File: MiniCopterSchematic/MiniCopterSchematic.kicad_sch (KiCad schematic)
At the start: 19 parts, among them J1 MPU6050_IMU, M1 MOTOR_DC_1, M2 MOTOR_DC_2, M3 MOTOR_DC_3, M4 MOTOR_DC_4, Q1 FQP20NO6L, Q2 FQP20NO6L, Q3 FQP20NO6L, Q4 FQP20NO6L

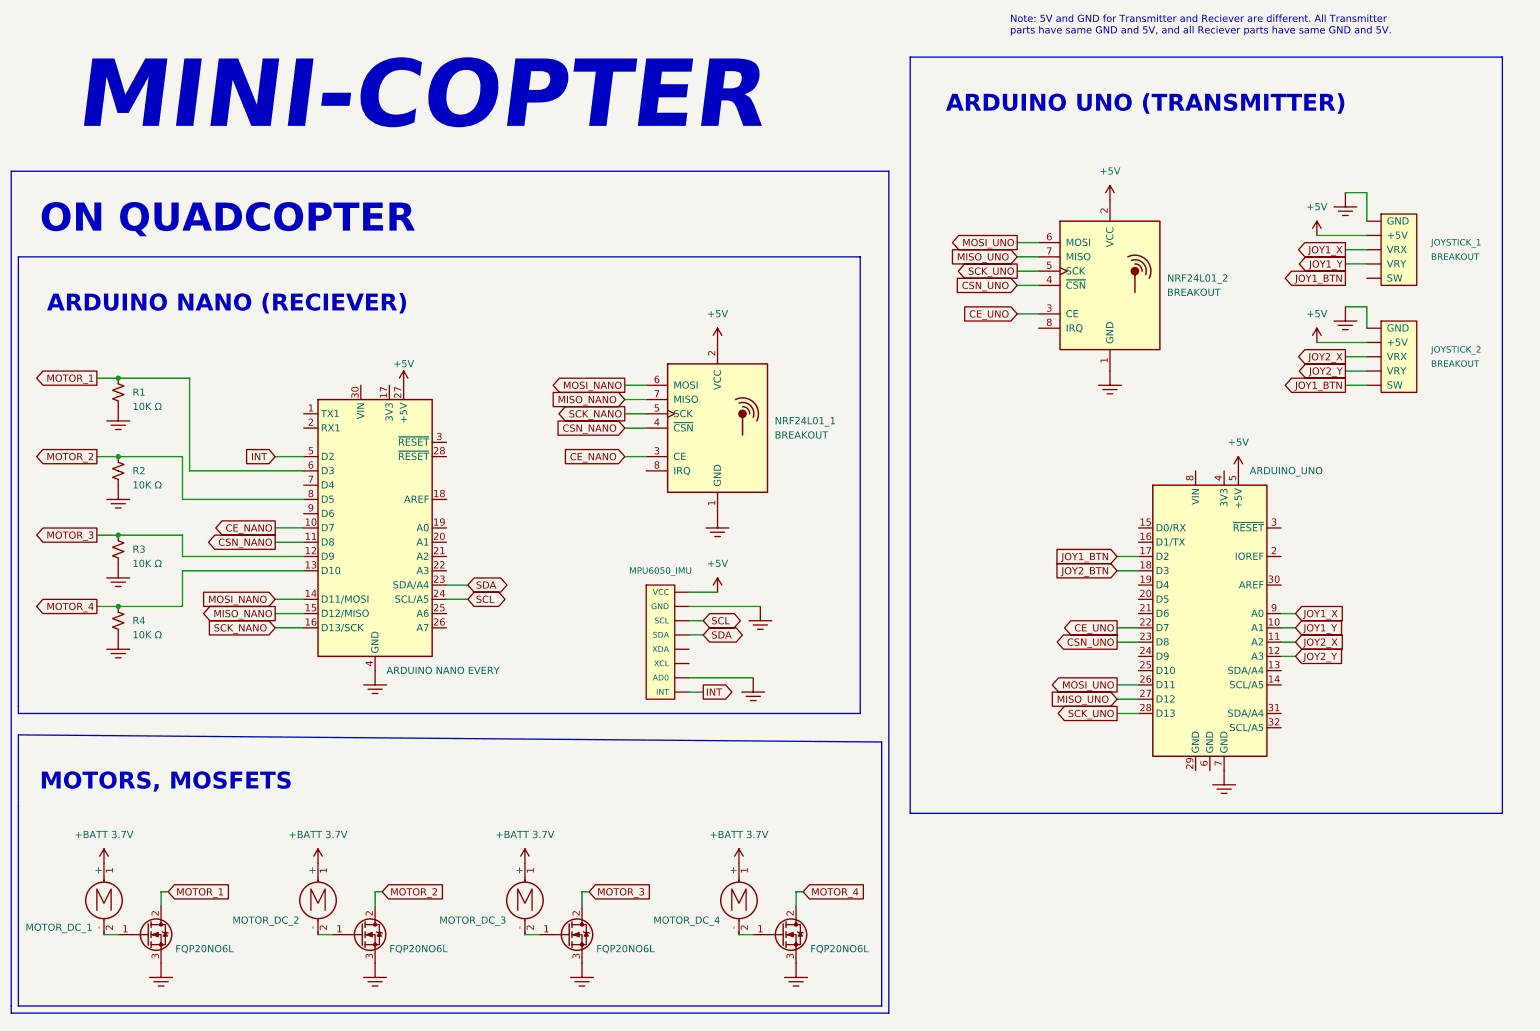
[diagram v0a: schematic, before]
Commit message: Updated schematic, added pictures, updated readme
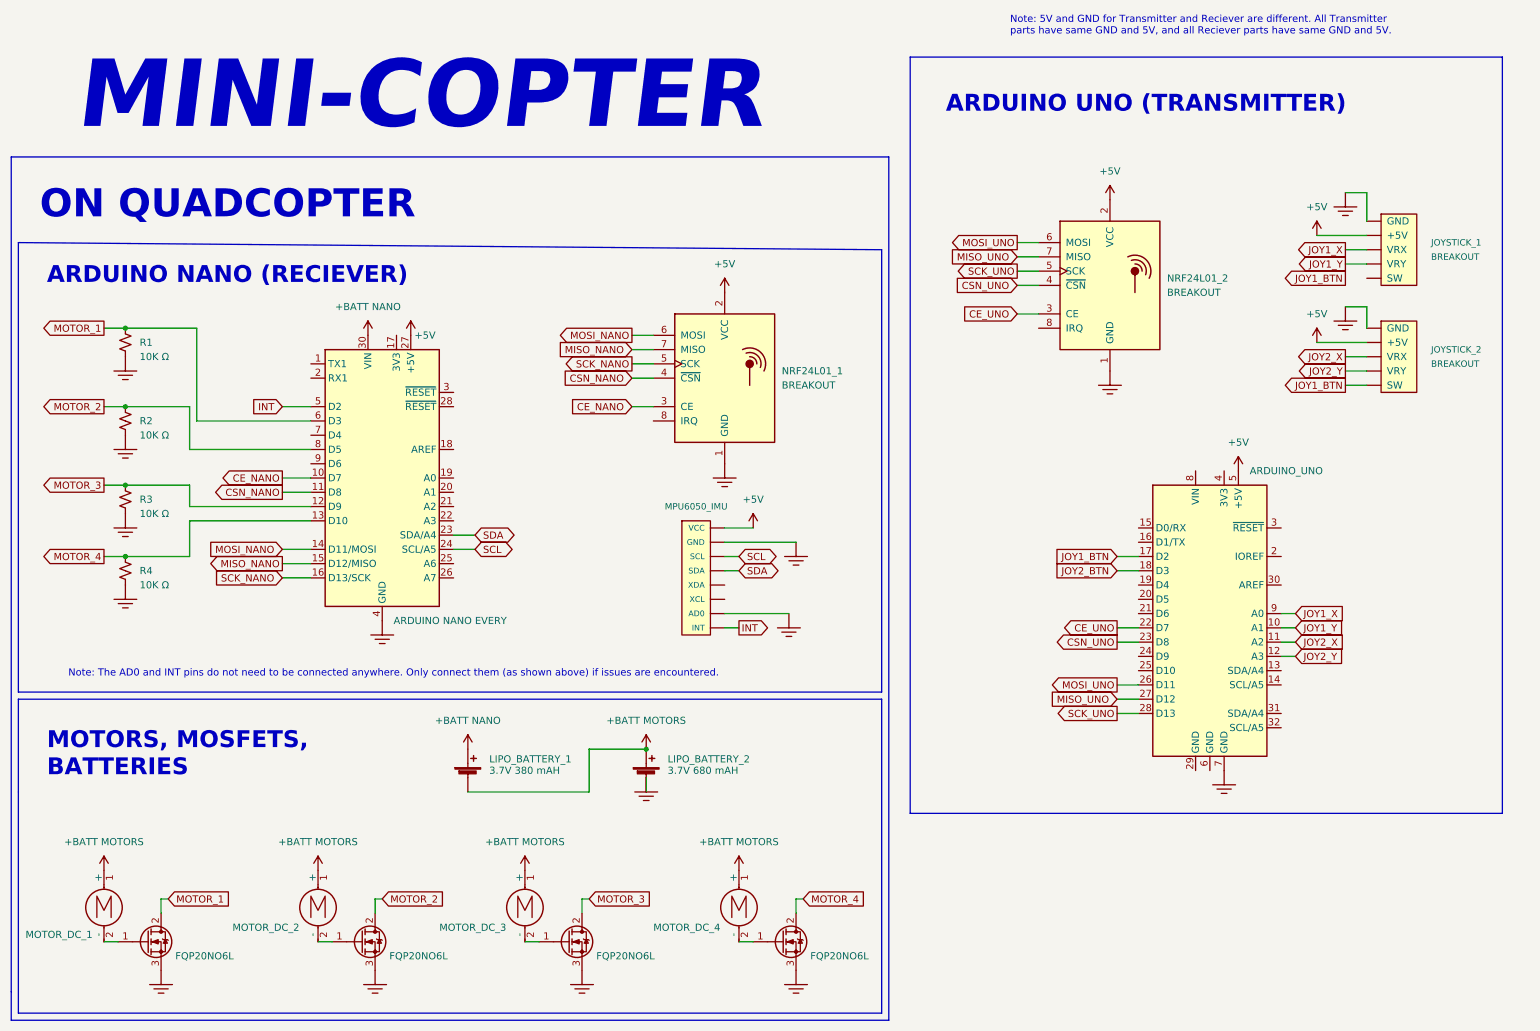
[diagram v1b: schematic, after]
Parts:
- added LIPO_BATTERY_1: 3.7V 380 mAH, symbol Device:Battery_Cell
- added LIPO_BATTERY_2: 3.7V 680 mAH, symbol Device:Battery_Cell
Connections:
- net +BATT: now also A1.30 (VIN), LIPO_BATTERY_1.1 (+), LIPO_BATTERY_1.2 (-), LIPO_BATTERY_2.1 (+)
- net GND: now also LIPO_BATTERY_2.2 (-)
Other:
- note added: "MOTORS, MOSFETS, BATTERIES"
- note added: "Note: The AD0 and INT pins do not need to be connected anywhere. Only connect them (as shown above) if issues are encountered."
- note removed: "MOTORS, MOSFETS"
- moved on the sheet: NRF24L01_1, R1, R2, R3, R4
